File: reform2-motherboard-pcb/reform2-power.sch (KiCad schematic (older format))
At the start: 196 parts, among them J1 Jack-DC, J13 BATCON1, J2 BATCON2, J22 LPC_IO, J23 KDBSYSCTL, J8 USB_B_Micro, Q1 Si7850DP, Q10 PMV50EPEAR, Q11 PMV50EPEAR, Q12 PMV50EPEAR, Q15 Si7850DP, Q17 Si7850DP, Q18 Si7461DP, Q2 Si7850DP, Q3 Si7461DP, Q5 PMV50EPEAR, Q6 PMV50EPEAR, Q7 PMV50EPEAR, Q8 PMV50EPEAR, Q9 PMV50EPEAR, SW1 SW_LPCPROG, SW2 SW_LPCRST, U12 LM2677SX-3.3, U13 TLV62568DBV, U14 LMR16006YQ3, U17 TLV1117-18, U18 LPC11U24FBD48-301, U19 TLV62568DBV, U2 LTC4020EUHFPBF, U4 LTC6803-4, U5 PCF8523T, U6 INA260, U7 LM2677SX-5, Y2 12MHz, Y4 32.768 kHz

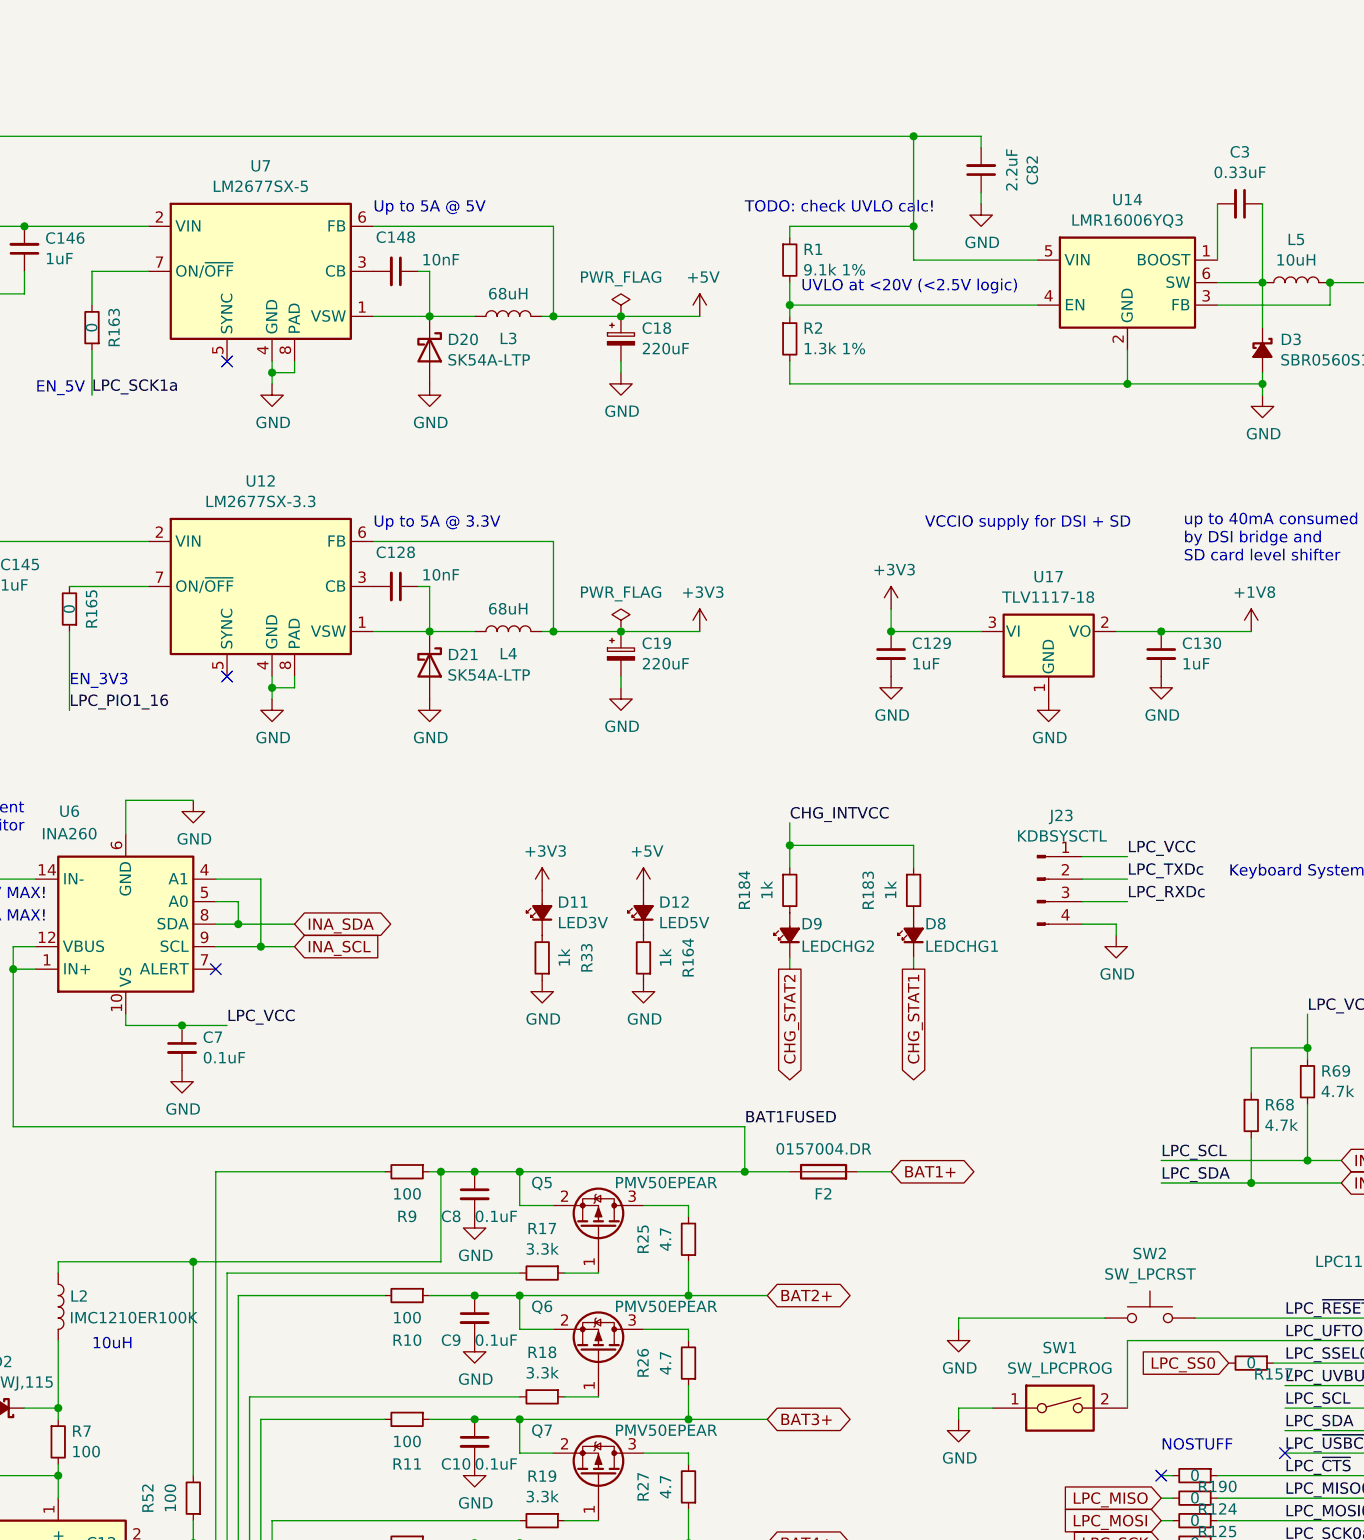
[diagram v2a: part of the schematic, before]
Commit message: reform2-motherboard 2d4 component cleanup
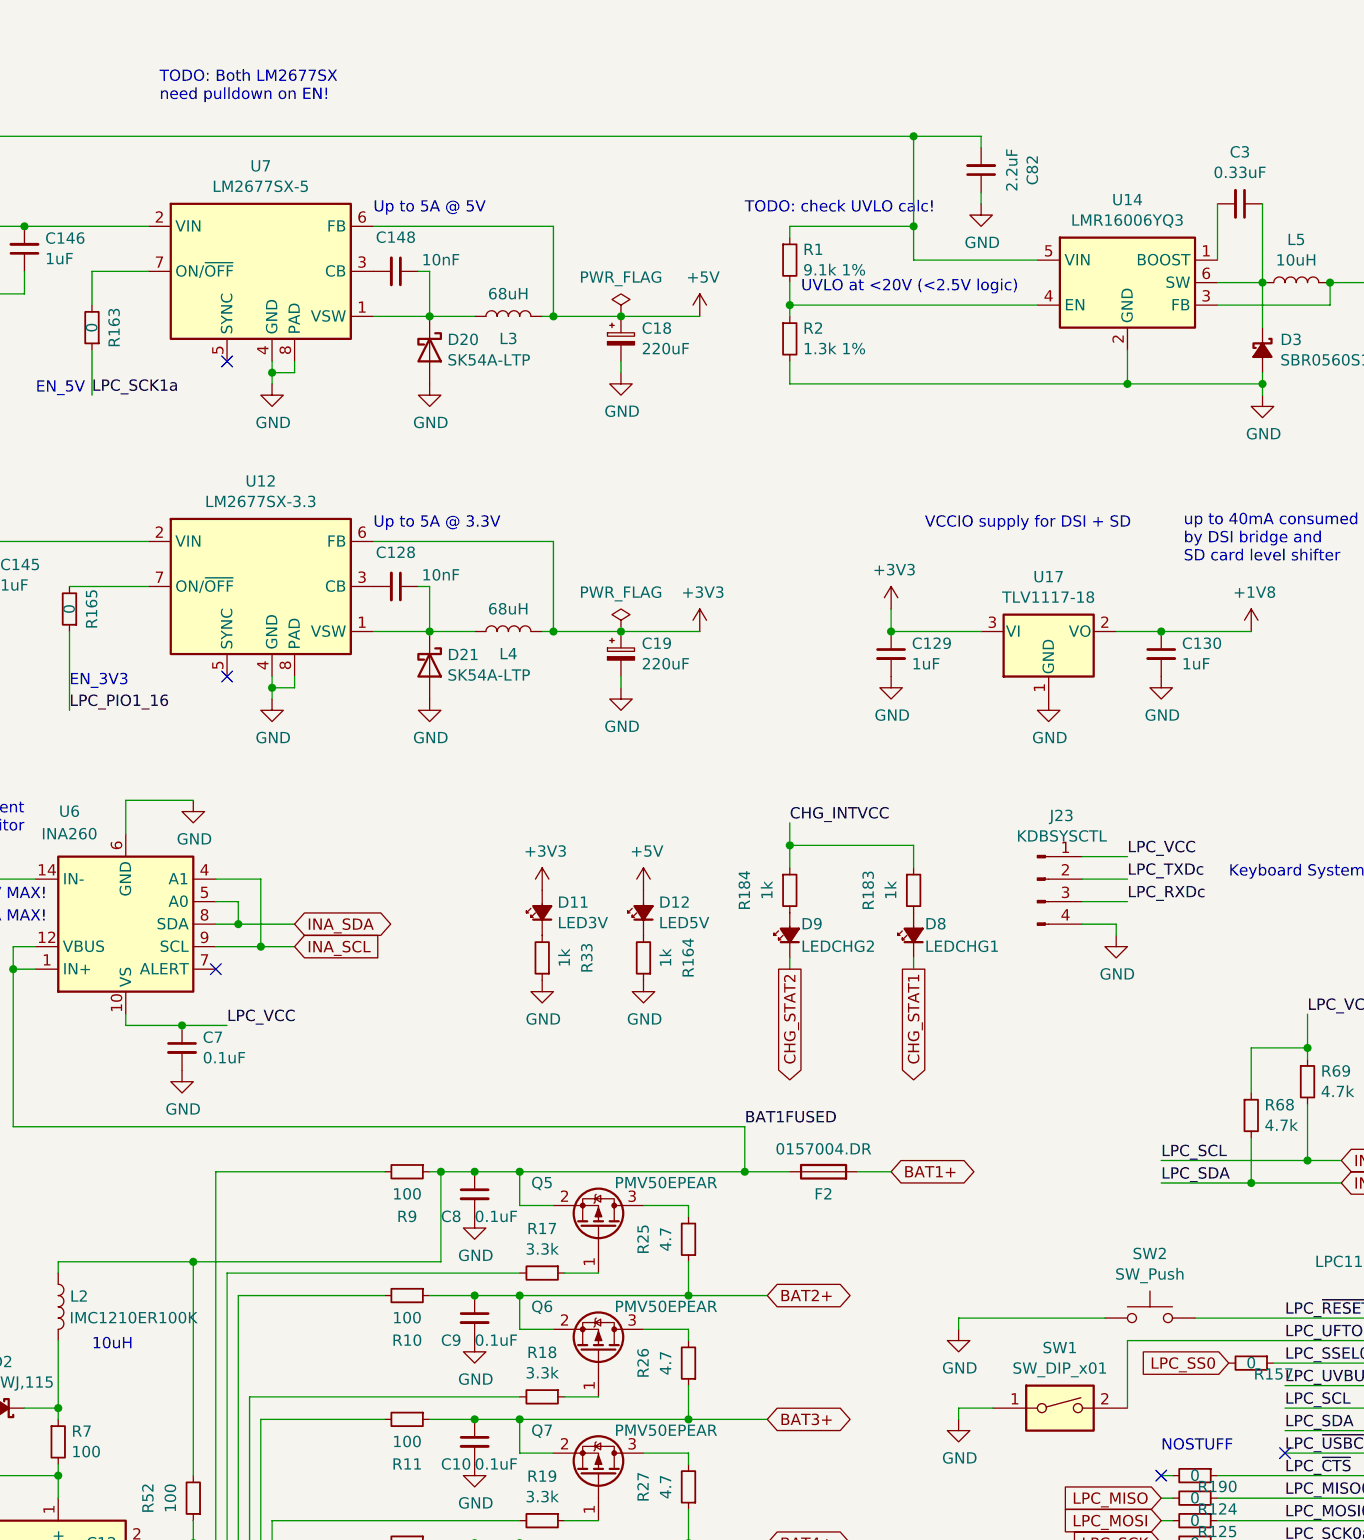
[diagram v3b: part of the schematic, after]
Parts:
- SW1: value SW_LPCPROG -> SW_DIP_x01; Manufacturer Omron -> Apem; Manufacturer_No A6S-1101-H -> DM01
- SW2: value SW_LPCRST -> SW_Push; Manufacturer CK -> C&K; Manufacturer_No KMR223NGULCLFG -> KMR221GLFS
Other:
- note added: "TODO: Both LM2677SX\nneed pulldown on EN!"
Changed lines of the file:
@@
 P 11450 6250
 F 0 "SW2" H 11450 6535 50  0000 C CNN
-F 1 "SW_LPCRST" H 11450 6444 50  0000 C CNN
+F 1 "SW_Push" H 11450 6444 50  0000 C CNN
 F 2 "Button_Switch_SMD:SW_Push_1P1T_NO_CK_KMR2" H 11450 6450 50  0001 C CNN
 F 3 "~" H 11450 6450 50  0001 C CNN
-F 4 "CK" H 11450 6250 50  0001 C CNN "Manufacturer"
-F 5 "KMR223NGULCLFG" H 11450 6250 50  0001 C CNN "Manufacturer_No"
+F 4 "C&K" H 11450 6250 50  0001 C CNN "Manufacturer"
+F 5 "KMR221GLFS" H 11450 6250 50  0001 C CNN "Manufacturer_No"
 F 6 "y" H 11450 6250 50  0001 C CNN "Checked"
 F 7 "Mouser" H 11450 6250 50  0001 C CNN "Distributor"
@@
 AR Path="/5CC81028/5DE51B0E" Ref="SW1"  Part="1"
 F 0 "SW1" H 11050 6917 50  0000 C CNN
-F 1 "SW_LPCPROG" H 11050 6826 50  0000 C CNN
+F 1 "SW_DIP_x01" H 11050 6826 50  0000 C CNN
 F 2 "Button_Switch_SMD:SW_DIP_SPSTx01_Slide_Omron_A6S-110x_W8.9mm_P2.54mm" H 11050 6650 50  0001 C CNN
 F 3 "~" H 11050 6650 50  0001 C CNN
-F 4 "Omron" H 11050 6650 50  0001 C CNN "Manufacturer"
-F 5 "A6S-1101-H" H 11050 6650 50  0001 C CNN "Manufacturer_No"
+F 4 "Apem" H 11050 6650 50  0001 C CNN "Manufacturer"
+F 5 "DM01" H 11050 6650 50  0001 C CNN "Manufacturer_No"
 F 6 "y" H 11050 6650 50  0001 C CNN "Checked"
 F 7 "Mouser" H 11050 6650 50  0001 C CNN "Distributor"
@@
 	0    1    1    0
 $EndComp
+Text Notes 7050 850  0    50   ~ 0
+TODO: Both LM2677SX\nneed pulldown on EN!
 $EndSCHEMATC

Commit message: reform2-motherboard: first R-1 snapshot. main changes: EMI, ESD, audio filter, enable FETs, SHDN fix, more rail switches
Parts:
- removed R162: 10k, Resistor_SMD:R_0603_1608Metric, symbol Device:R_Small
- removed R163, R165, R190: 0, Resistor_SMD:R_0603_1608Metric, symbol Device:R_Small
- removed R2: 1.3k 1%, Resistor_SMD:R_0603_1608Metric, symbol Device:R_Small
- added D13: SMAJ36CA-E3/5A, Diode_SMD:D_SMA, symbol Device:D_Schottky
- added Q13, Q14, Q4: PMV50ENEA, Package_TO_SOT_SMD:SOT-23, symbol Transistor_FET:2N7002E
- added R34: 150k, Resistor_SMD:R_0603_1608Metric, symbol Device:R_Small
- added R88, R89, R94: 100k, Resistor_SMD:R_0603_1608Metric, symbol Device:R_Small
- added R95: 10k, Resistor_SMD:R_0603_1608Metric, symbol Device:R_Small
- R1: value 9.1k 1% -> 0; Manufacturer Yageo -> Vishay Dale; Manufacturer_No RC0603FR-079K1L -> CRCW06030000Z0EAC
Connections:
- net 30V_GATE: now also R1.2; no longer R1.1
- net CHG_INTVCC: now also U2.10 (VIN_REG); no longer R193.1
- net CHG_RNG: now also Q4.1 (G), R95.2; no longer R53.1
- net GND: now also R193.1, D13.2 (A), Q13.2 (S), Q14.2 (S), Q4.2 (S), R94.1, R95.1; no longer U2.11 (MODE)
- net LPC_PIO1_16: now also Q14.1 (G), R89.1
- net LPC_SCK1a: now also Q13.1 (G), R88.1
- net LPC_VCC: now also R88.2, R89.2
- net at U12.7 (ON/~OFF~): now also Q14.3 (D)
- net at U7.7 (ON/~OFF~): now also Q13.3 (D)
- net at U14.4 (EN): now also R1.1; no longer R1.2
- net at C149.1, D1.1 (K), F1.2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: now also D13.1 (K)
- net at U2.9 (~SHDN): now also R34.1, R94.2
- net at R193.2: now also U2.11 (MODE); no longer U2.10 (VIN_REG)
- net at C160.1, C161.1, C44.2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: now also R34.2
- net LPC_PIO1_31: no longer names the net of J22.12 (Pin_12)
- net LPC_PIO1_31: no longer U18.25 (PIO1_31)
- net LPC_~CTS renamed AUX_PWR_EN
- net PCIE1_PWR renamed PCIE1_PWR_EN
- new net: Q4.3 (D), R53.1
- new net USB_PWR_EN: U18.25 (PIO1_31)
- no-connect marks 10 -> 9
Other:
- note added: "standby always-on\npower rail"
- note removed: "FIXME: confirm\ntemperature stress\nof balancing Rs"
- note removed: "TODO: Both LM2677SX\nneed pulldown on EN!"
- note removed: "TODO: check UVLO calc!"
- note removed: "UVLO at <20V (<2.5V logic)"
- moved on the sheet: C121, C122, C125, C145, C146, C16, C17, C18, C19, C3, C44, C64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

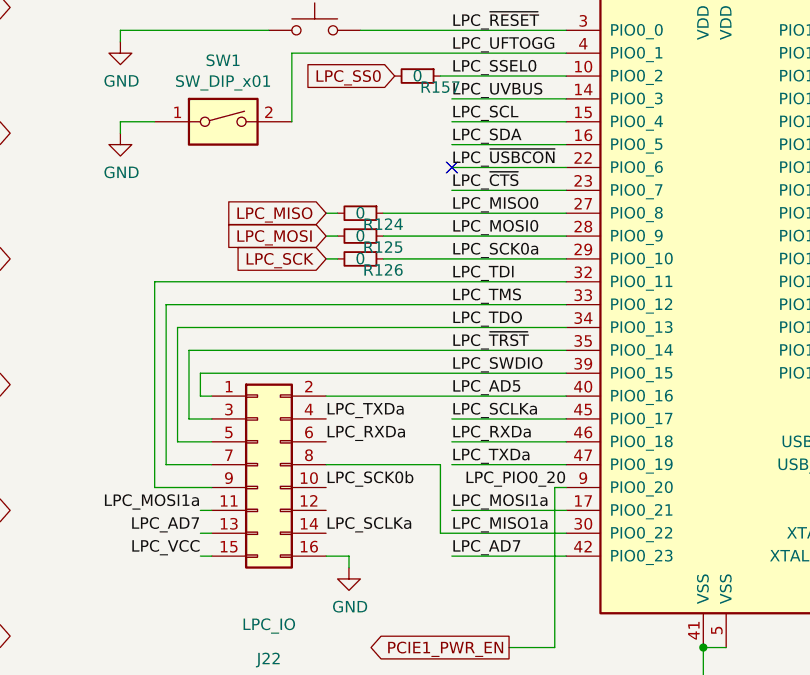
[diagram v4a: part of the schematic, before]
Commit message: reform2-motherboard: R-1 silkscreen cleanup; usb hub reset pulldown added
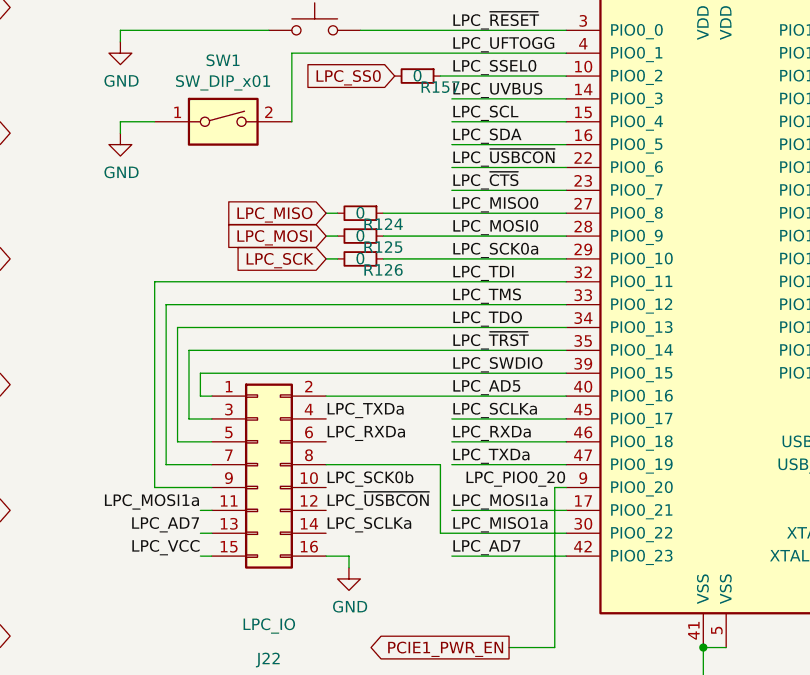
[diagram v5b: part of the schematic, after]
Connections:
- net LPC_~USBCON: now also J22.12 (Pin_12)
- no-connect marks 9 -> 8
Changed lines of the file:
@@
 Text Label 12050 7050 0    50   ~ 0
 LPC_MISO0
-Text Label 12050 6850 0    50   ~ 0
-LPC_~USBCON
 Wire Wire Line
 	12550 6850 12050 6850
@@
 NOSTUFF
 NoConn ~ 14950 7850
-NoConn ~ 12050 6850
 Wire Wire Line
 	8200 3000 8250 3000
@@
 Wire Wire Line
 	1400 1300 2250 1300
+Text Label 12050 6850 0    50   ~ 0
+LPC_~USBCON
+Text Label 11500 8350 0    50   ~ 0
+LPC_~USBCON
 $EndSCHEMATC
